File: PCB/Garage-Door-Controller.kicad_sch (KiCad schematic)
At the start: 35 parts, among them J1 USB_C_Receptacle_USB2.0_16P, J2 Conn_01x07_Pin, J3 Conn_01x07_Pin, J4 Screw_Terminal_01x04, SW1 TS-1088-AR02016, SW2 TS-1088-AR02016, U1 ESP32-C3-MINI-1, U2 AMS1117-3.3, U3 LTV-817S-TA1-C

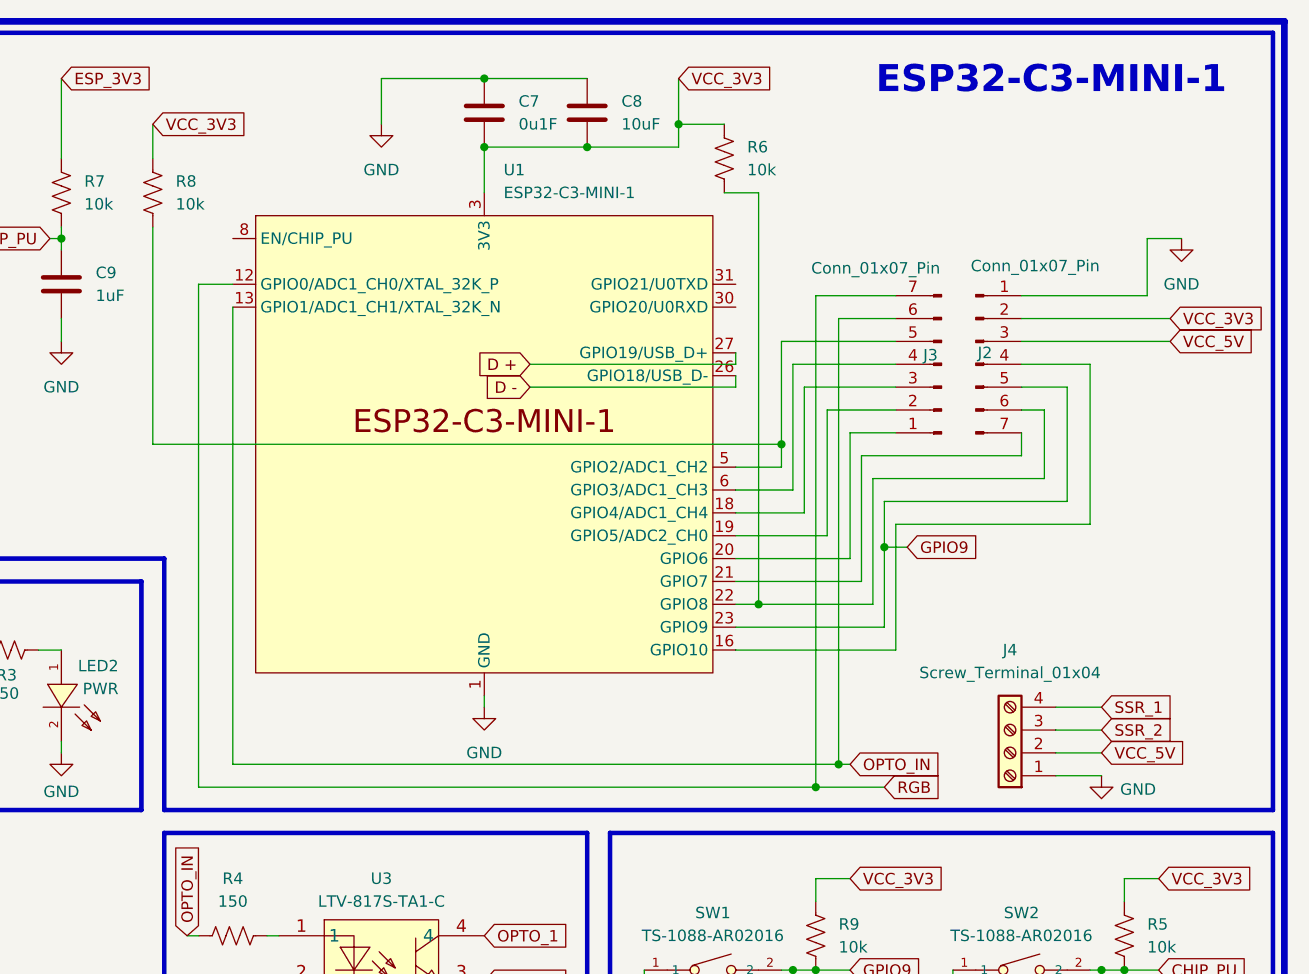
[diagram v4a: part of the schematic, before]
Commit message: Split terminals into 2 blocks
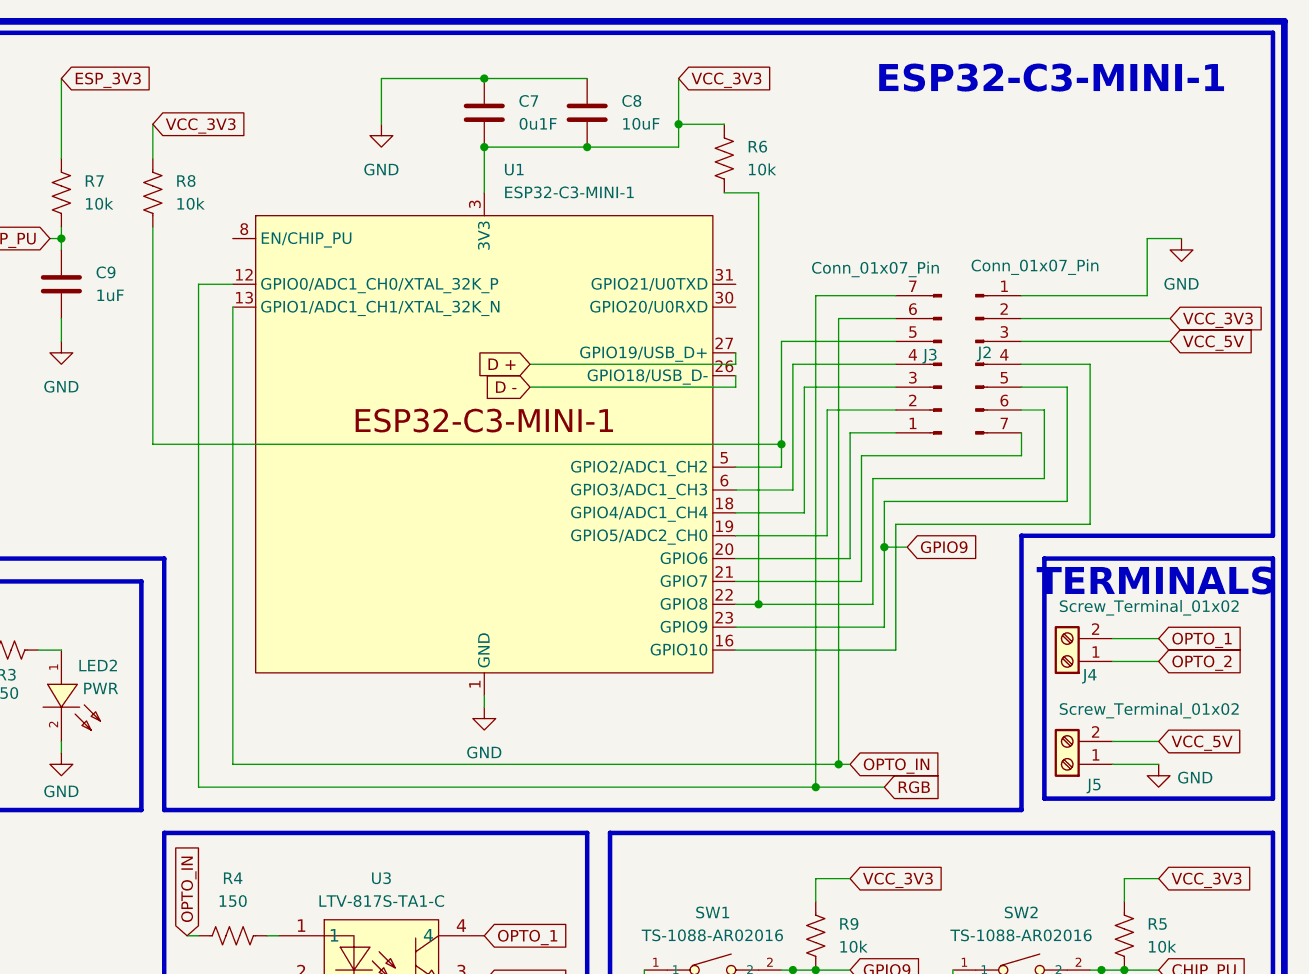
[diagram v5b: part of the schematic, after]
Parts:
- removed J4: Screw_Terminal_01x04, TerminalBlock_Phoenix:TerminalBlock_Phoenix_MKDS-1,5-4-5.08_1x04_P5.08mm_Horizontal, symbol Connector:Screw_Terminal_01x04
- added J4, J5: Screw_Terminal_01x02, TerminalBlock_Phoenix:TerminalBlock_Phoenix_MKDS-1,5-2-5.08_1x02_P5.08mm_Horizontal, symbol Connector:Screw_Terminal_01x02
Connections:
- net GND: now also J5.1 (Pin_1)
- net OPTO_1: now also J4.2 (Pin_2)
- net OPTO_2: now also J4.1 (Pin_1)
- net VCC_5V: now also J5.2 (Pin_2)
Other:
- note added: "TERMINALS"
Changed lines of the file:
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@@
 	)
 	(rectangle
+		(start 257.81 72.39)
+		(end 283.21 99.06)
+		(stroke
+			(width 0.5)
+			(type solid)
+		)
+		(fill
+			(type none)
+		)
+	)
+	(rectangle
 		(start 209.55 102.87)
 		(end 283.21 133.35)
@@
 		)
 	)
+	(text "TERMINALS"
+		(exclude_from_sim no)
+		(at 270.256 75.184 0)
+		(effects
+			(font
+				(size 3 3)
+				(thickness 0.6)
+				(bold yes)
+			)
+		)
+	)
 	(text "Optocoupler"
 		(exclude_from_sim no)
@@
 	(wire
 		(pts
-			(xy 259.08 88.9) (xy 264.16 88.9)
+			(xy 265.43 81.28) (xy 270.51 81.28)
 		)
 		(stroke
@@
 		)
 	)
-	(polyline
-		(pts
-			(xy 283.21 13.97) (xy 283.21 100.33)
-		)
-		(stroke
-			(width 0.5)
-			(type solid)
-		)
-	)
 	(wire
 		(pts
@@
 		)
 	)
+	(polyline
+		(pts
+			(xy 255.27 100.33) (xy 255.27 69.85)
+		)
+		(stroke
+			(width 0.5)
+			(type solid)
+		)
+	)
 	(wire
 		(pts
@@
 	(wire
 		(pts
-			(xy 259.08 96.52) (xy 264.16 96.52)
+			(xy 265.43 95.25) (xy 270.51 95.25)
 		)
 		(stroke
@@
 	(wire
 		(pts
-			(xy 259.08 91.44) (xy 264.16 91.44)
+			(xy 265.43 83.82) (xy 270.51 83.82)
 		)
 		(stroke
@@
 	(polyline
 		(pts
-			(xy 283.21 100.33) (xy 160.02 100.33)
+			(xy 255.27 100.33) (xy 160.02 100.33)
 		)
 		(stroke
@@
 		)
 	)
+	(polyline
+		(pts
+			(xy 283.21 69.85) (xy 283.21 13.97)
+		)
+		(stroke
+			(width 0.5)
+			(type solid)
+		)
+	)
 	(wire
 		(pts
@@
 		)
 	)
+	(polyline
+		(pts
+			(xy 255.27 69.85) (xy 283.21 69.85)
+		)
+		(stroke
+			(width 0.5)
+			(type solid)
+		)
+	)
 	(wire
 		(pts
@@
 	(wire
 		(pts
-			(xy 259.08 93.98) (xy 264.16 93.98)
+			(xy 265.43 92.71) (xy 270.51 92.71)
 		)
 		(stroke
@@
 		)
 	)
-	(global_label "SSR_2"
+	(global_label "OPTO_2"
 		(shape input)
-		(at 264.16 91.44 0)
+		(at 270.51 83.82 0)
 		(fields_autoplaced yes)
 		(effects
@@
 		)
 		(property "Intersheetrefs" "${INTERSHEET_REFS}"
-			(at 273.0113 91.44 0)
+			(at 280.5709 83.82 0)
 			(hide yes)
 			(show_name no)
@@
 		)
 	)
-	(global_label "SSR_1"
+	(global_label "OPTO_1"
 		(shape input)
-		(at 264.16 88.9 0)
+		(at 270.51 81.28 0)
 		(fields_autoplaced yes)
 		(effects
@@
 		)
 		(property "Intersheetrefs" "${INTERSHEET_REFS}"
-			(at 273.0113 88.9 0)
+			(at 280.5709 81.28 0)
 			(hide yes)
 			(show_name no)
@@
 	(global_label "VCC_5V"
 		(shape input)
-		(at 264.16 93.98 0)
+		(at 270.51 92.71 0)
 		(fields_autoplaced yes)
 		(effects
@@
 		)
 		(property "Intersheetrefs" "${INTERSHEET_REFS}"
-			(at 274.0395 93.98 0)
+			(at 280.3895 92.71 0)
 			(hide yes)
 			(show_name no)
@@
 	(symbol
 		(lib_id "power:GND")
-		(at 264.16 96.52 0)
+		(at 270.51 95.25 0)
 		(unit 1)
 		(body_style 1)
@@
 		(dnp no)
 		(property "Reference" "#PWR012"
-			(at 264.16 102.87 0)
+			(at 270.51 101.6 0)
 			(hide yes)
 			(show_name no)
@@
 		)
 		(property "Value" "GND"
-			(at 268.224 98.044 0)
+			(at 274.574 96.774 0)
 			(show_name no)
 			(do_not_autoplace no)
@@
 		)
 		(property "Footprint" ""
-			(at 264.16 96.52 0)
+			(at 270.51 95.25 0)
 			(hide yes)
 			(show_name no)
@@
 		)
 		(property "Datasheet" ""
-			(at 264.16 96.52 0)
+			(at 270.51 95.25 0)
 			(hide yes)
 			(show_name no)
@@
 		)
 		(property "Description" "Power symbol creates a global label with name \"GND\" , ground"
-			(at 264.16 96.52 0)
+			(at 270.51 95.25 0)
 			(hide yes)
 			(show_name no)
@@
 	)
 	(symbol
+		(lib_id "Connector:Screw_Terminal_01x02")
+		(at 260.35 95.25 180)
+		(unit 1)
+		(body_style 1)
+		(exclude_from_sim no)
+		(in_bom yes)
+		(on_board yes)
+		(in_pos_files yes)
+		(dnp no)
+		(property "Reference" "J5"
+			(at 263.398 97.536 0)
+			(show_name no)
+			(do_not_autoplace no)
+			(effects
+				(font
+					(size 1.27 1.27)
+				)
+			)
+		)
+		(property "Value" "Screw_Terminal_01x02"
+			(at 269.494 89.154 0)
+			(show_name no)
+			(do_not_autoplace no)
+			(effects
+				(font
+					(size 1.27 1.27)
+				)
+			)
+		)
+		(property "Footprint" "TerminalBlock_Phoenix:TerminalBlock_Phoenix_MKDS-1,5-2-5.08_1x02_P5.08mm_Horizontal"
+			(at 260.35 95.25 0)
+			(hide yes)
+			(show_name no)
+			(do_not_autoplace no)
+			(effects
+				(font
+					(size 1.27 1.27)
+				)
+			)
+		)
+		(property "Datasheet" ""
+			(at 260.35 95.25 0)
+			(hide yes)
+			(show_name no)
+			(do_not_autoplace no)
+			(effects
+				(font
+					(size 1.27 1.27)
+				)
+			)
+		)
+		(property "Description" "Generic screw terminal, single row, 01x02, script generated (kicad-library-utils/schlib/autogen/connector/)"
+			(at 260.35 95.25 0)
+			(hide yes)
+			(show_name no)
+			(do_not_autoplace no)
+			(effects
+				(font
+					(size 1.27 1.27)
+				)
+			)
+		)
+		(pin "2"
+		)
+		(pin "1"
+		)
+		(instances
+			(project "Garage-Door-Controller"
+				(path "/8b0ce9a6-853b-4e12-ac4b-f9d95766b3f3"
+					(reference "J5")
+					(unit 1)
+				)
+			)
+		)
+	)
+	(symbol
 		(lib_id "power:GND")
 		(at 171.45 121.92 0)
@@
 	)
 	(symbol
+		(lib_id "Connector:Screw_Terminal_01x02")
+		(at 260.35 83.82 180)
+		(unit 1)
+		(body_style 1)
+		(exclude_from_sim no)
+		(in_bom yes)
+		(on_board yes)
+		(in_pos_files yes)
+		(dnp no)
+		(property "Reference" "J4"
+			(at 262.89 85.344 0)
+			(show_name no)
+			(do_not_autoplace no)
+			(effects
+				(font
+					(size 1.27 1.27)
+				)
+			)
+		)
+		(property "Value" "Screw_Terminal_01x02"
+			(at 269.494 77.724 0)
+			(show_name no)
+			(do_not_autoplace no)
+			(effects
+				(font
+					(size 1.27 1.27)
+				)
+			)
+		)
+		(property "Footprint" "TerminalBlock_Phoenix:TerminalBlock_Phoenix_MKDS-1,5-2-5.08_1x02_P5.08mm_Horizontal"
+			(at 260.35 83.82 0)
+			(hide yes)
+			(show_name no)
+			(do_not_autoplace no)
+			(effects
+				(font
+					(size 1.27 1.27)
+				)
+			)
+		)
+		(property "Datasheet" ""
+			(at 260.35 83.82 0)
+			(hide yes)
+			(show_name no)
+			(do_not_autoplace no)
+			(effects
+				(font
+					(size 1.27 1.27)
+				)
+			)
+		)
+		(property "Description" "Generic screw terminal, single row, 01x02, script generated (kicad-library-utils/schlib/autogen/connector/)"
+			(at 260.35 83.82 0)
+			(hide yes)
+			(show_name no)
+			(do_not_autoplace no)
+			(effects
+				(font
+					(size 1.27 1.27)
+				)
+			)
+		)
+		(pin "2"
+		)
+		(pin "1"
+		)
+		(instances
+			(project "Garage-Door-Controller"
+				(path "/8b0ce9a6-853b-4e12-ac4b-f9d95766b3f3"
+					(reference "J4")
+					(unit 1)
+				)
+			)
+		)
+	)
+	(symbol
 		(lib_id "Device:C")
 		(at 104.14 48.26 0)
@@
 					(unit 1)
 				)
-			)
-		)
-	)
-	(symbol
-		(lib_id "Connector:Screw_Terminal_01x04")
-		(at 254 93.98 180)
-		(unit 1)
-		(body_style 1)
-		(exclude_from_sim no)
-		(in_bom yes)
-		(on_board yes)
-		(in_pos_files yes)
-		(dnp no)
-		(fields_autoplaced yes)
-		(property "Reference" "J4"
-			(at 254 82.55 0)
-			(show_name no)
-			(do_not_autoplace no)
-			(effects
-				(font
-					(size 1.27 1.27)
-				)
-			)
-		)
-		(property "Value" "Screw_Terminal_01x04"
-			(at 254 85.09 0)
-			(show_name no)
-			(do_not_autoplace no)
-			(effects
-				(font
-					(size 1.27 1.27)
-				)
-			)
-		)
-		(property "Footprint" "TerminalBlock_Phoenix:TerminalBlock_Phoenix_MKDS-1,5-4-5.08_1x04_P5.08mm_Horizontal"
-			(at 254 93.98 0)
-			(hide yes)
-			(show_name no)
-			(do_not_autoplace no)
-			(effects
-				(font
-					(size 1.27 1.27)
-				)
-			)
-		)
-		(property "Datasheet" ""
-			(at 254 93.98 0)
-			(hide yes)
-			(show_name no)
-			(do_not_autoplace no)
-			(effects
-				(font
-					(size 1.27 1.27)
-				)
-			)
-		)
-		(property "Description" "Generic screw terminal, single row, 01x04, script generated (kicad-library-utils/schlib/autogen/connector/)"
-			(at 254 93.98 0)
-			(hide yes)
-			(show_name no)
-			(do_not_autoplace no)
-			(effects
-				(font
-					(size 1.27 1.27)
-				)
-			)
-		)
-		(pin "1"
-		)
-		(pin "3"
-		)
-		(pin "4"
-		)
-		(pin "2"
-		)
-		(instances
-			(project "Garage-Door-Controller"
-				(path "/8b0ce9a6-853b-4e12-ac4b-f9d95766b3f3"
-					(reference "J4")
-					(unit 1)
-				)

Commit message: Fixed USB-C symbol
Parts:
- removed J1: USB_C_Receptacle_USB2.0_16P, lcsc_footprints:C53436595_USB-TYPE-C-SMD_JS16T-TYPE-C057-H730, symbol Connector:USB_C_Receptacle_USB2.0_16P
- added SW3: PWR, lcsc_footprints:C22435661_SW-SMD_MSK12C02G15-B, symbol lcsc_imported:MSK12C02G15-B
- added USB1: HYCW523-USBC16-735B, lcsc_footprints:C53436595_USB-TYPE-C-SMD_JS16T-TYPE-C057-H730, symbol lcsc_imported:HYCW523-USBC16-735B
- J4, J5: now left out of the parts list
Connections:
- net ESP_3V3 is gone; now on net VCC_3V3: R7.2
- net CHIP_PU: now also U1.8 (EN/CHIP_PU)
- net D +: now also USB1.A6 (DP1), USB1.B6 (DP2)
- net D -: now also USB1.A7 (DN1), USB1.B7 (DN2)
- net GND: now also SW3.4, SW3.5, USB1.1, USB1.2, USB1.3, USB1.4, USB1.A1B12 (GND), USB1.B1A12 (GND)
- net VCC_5V: now also SW3.1; no longer C1.1, C2.1, U2.3 (VI)
- net at D1.2 (A), D5.2 (A2): now also USB1.A4B9 (VBUS), USB1.B4A9 (VBUS)
- net at R2.2: now also USB1.A5 (CC1)
- net at R1.2: now also USB1.B5 (CC2)
- new net PWR_IN: C1.1, C2.1, SW3.2, U2.3 (VI)
- no-connect marks 3 -> 4
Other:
- note added: "Power Switch"
- note added: "Terminals"
- note removed: "TERMINALS"

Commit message: First export
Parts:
- C1, C12, C3, C6, C7: LCSC (none) -> C14663
- C10, C11: LCSC (none) -> C1653
- C2, C4, C8: LCSC (none) -> C15850
- C9: LCSC (none) -> C15849
- D1: LCSC (none) -> C82544
- D5, D6, D7: LCSC (none) -> C7433850
- R1, R2: LCSC (none) -> C27834
- R3, R4: LCSC (none) -> C17471
- R5, R6, R7, R8, R9: LCSC (none) -> C25804
- U1: LCSC (none) -> C2838502
- U2: LCSC (none) -> C6186
